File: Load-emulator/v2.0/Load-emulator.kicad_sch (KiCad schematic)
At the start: 29 parts, among them J1 2053380002, J10 533980871, J11 533980871, J12 2053380002, J13 2053380002, J14 2053380002, J2 2053380002, J3 2053380002, J4 2053380002, J5 SSW-126-01-G-D, J7 532610471, J8 SSW-126-01-G-D, Q11 NMOS, U6 LM318H

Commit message: [v2.0 - WIP] Update some things
[UPDATED]
- Added all Schematics;
- Changed the PCB size to be 10x20;
- Updated MOSFETs assignments;
- Added heatsinks;
- Changed order on the Picoblade;
- Small file clean up;
- And some more...

[TO DO]
- Fix/Research how to do the RSense stuff;
- Verify if we still need the -10V;
- Verify this VBus/VBat;
- Verify the difference of EPS2 and EPS²RE radio voltage (6V/5V);
- Complete the entire PCB layout; [! IMPORTANT !]
- Do a better clean up of the files;
- And some more...
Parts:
- removed Q11: NMOS, symbol Simulation_SPICE:NMOS
- removed R4, R5, R6, R7, R8, R9: 0R, symbol Device:R
- removed U6: LM318H, symbol Amplifier_Operational:LM318H
- added HS1: 573100D00000G, symbol Mechanical:Heatsink
- added J1: 2053380002, footprints:2053380002, symbol 2053380002:2053380002
- added Q1: RD3L08DBLHRB, footprints:TRANS_RD3L08DBLHRB, symbol RD3L08DBLHRB:RD3L08DBLHRB
- added U0: LT1492, symbol Amplifier_Operational:LT1492
- C1, C2, R2, R3: now left out of the parts list
- J10: renamed from J8; footprint SSW-126-01-G-D:SAMTEC_SSW-126-01-G-D -> footprints:SAMTEC_SSW-126-01-G-D
- J12: renamed from J11; now left out of the parts list
- J9: renamed from J5; footprint SSW-126-01-G-D:SAMTEC_SSW-126-01-G-D -> footprints:SAMTEC_SSW-126-01-G-D
- J99: renamed from J7; now left out of the parts list
- R1: renamed from R52; now left out of the parts list
- renumbered J10 to J11, J1 to J2, J2 to J3, J3 to J4, J4 to J5, J12 to J6, J13 to J7, J14 to J8
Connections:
- net 3V3_Deployment_ANT is gone; now on net R-3V3_AntDep: J10.35, J10.36
- net 3V3_EPS_Beacon is gone; now on net R-3V3_Beacon_TTC: J10.27, J10.28
- net 5V_Radio_0 is gone; now on net R-5V0_Payload: J3.2, J9.49, J9.50
- net Earth is gone; now on net GND: C1.2, C2.2, R1.2
- net Vbat is gone; now on net R-Vbat: J2.2
- net +10V: now also J99.1, J1.1; no longer J99.2
- net -10V: now also J99.2; no longer J99.1
- net 3V3/1A: now also J12.6; no longer J12.4
- net 3V3/2A: now also J12.4; no longer J12.6
- net 5V/3A: now also J12.3; no longer J12.7
- net 7.4V/0.592A: now also J12.7; no longer J12.3
- net Control: now also U0.3 (+)
- net EPS: now also Q1.2
- net GND: now also J1.2
- net at R1.1: now also Q1.3, U0.2 (-)
- net 3V3_AntDep renamed R-3V3_AntDep
- net 3V3_Beacon renamed R-3V3_Beacon_TTC
- net 3V3_OBDH renamed R-3V3_OBDH
- net 5V0_RadioBeacon renamed R-5V0_RadioBeacon
- net 5V0_RadioMain renamed R-5V0_Payload
- net 5V_Payload renamed S-5V_Payload
- net 6V_Radio_1 renamed S-6V_Radio_1
- net VBus renamed R-Vbat
- new net: Q1.1, U0.1
- no-connect marks 84 -> 82
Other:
- sheet Filter_and_CurrentSink_6x500mA renamed Filter_and_CurrentSink_1x3A
- removed sheet Current Sink 500mA
- removed sheet Low-Pass_Filter_1
- added sheet Filter_and_CurrentSink_1x1A (Filter_and_CurrentSink_1x1A.kicad_sch)
- added sheet Filter_and_CurrentSink_1x1A1 (Filter_and_CurrentSink_1x1A.kicad_sch)
- added sheet Filter_and_CurrentSink_1x3A_1 (Filter_and_CurrentSink_3x1A.kicad_sch)
- added sheet Filter_and_CurrentSink_1x3A_2 (Filter_and_CurrentSink_3x1A.kicad_sch)
- added sheet Filter_and_CurrentSink_2x1A (Filter_and_CurrentSink_2x1A.kicad_sch)
- added sheet Filter_and_CurrentSink_2x1A1 (Filter_and_CurrentSink_2x1A.kicad_sch)
- sheet Filter_and_CurrentSink_1x3A: file Filter_and_CurrentSink_6x500mA.kicad_sch -> Filter_and_CurrentSink_3x1A.kicad_sch
- note added: "1A -> 1 mm 2A -> 1,5 mm 3A -> 2 mm"
- note added: "1A MAX"
- note added: "5V from Radio of ESP²RE"
- note added: "< NEED CONFIRMATION"
- note added: "< R-5V0_RadioBeacon ???"
- note added: "Channel 1 - 6V_Radio_1 (6V/3A)/(5V/3A) Channel 2 - 5V_Radio_0 (5V/3A) Channel 3 - 5V_Payload (5V/3A) Channel 4 - 3V3_Beacon_TTC (3V3/2A) Channel 5 - 3V3_Deployment_ANT (3V3/2A) Channel 6 - 3V3_OBDH (3V3/1A) Channel 7 - VBus (7.4V/0,592A) Channel 8 - GND"
- note added: "POWER"
- note added: "REVIEW THE WIDTH > OF THE TRACES"
- note added: "RSense = Vcontrol/Ieps"
- note added: "Schematic of EPS²RE"
- note added: "V - Verify if we still need -10V"
- note added: "We got two different voltages one from EPS and another from EPS²RE the 6V Radio 1 is 6V, meanwhile the two voltages outputs for the Radio from the ESP²RE is 5V."
- note removed: "1A -> 0,22mm 2A -> 0,57mm 3A -> 1mm"
- note removed: "5V do Radio do ESP²RE +"
- note removed: "< Definir um MOSFET"
- note removed: "<- TTC"
- note removed: "<----------TTC"
- note removed: "Channel 1 - 6V_Radio_1 (6V/3A) Channel 2 - 5V_Radio_0 (5V/3A) Channel 3 - VBus (7.4V/0,592A) Channel 4 - 3V3_OBDH (3V3/1A) Channel 5 - 3V3_Deployment_ANT (3V3/2A) Channel 6 - 3V3_EPS_Beacon (3V3/2A) Channel 7 - 5V_Payload (5V/3A) Channel 8 - GND"
- note removed: "Enable Pin"
- note removed: "GND"
- note removed: "Ieps = Vcontrol/Rsense"
- note removed: "MUDAR ESSE AMPOP PARA LT1492"
- note removed: "Obs: After reduction, max current -> 3A"
- note removed: "Precisa dessa informacao?"
- note removed: "Temos duas tensões diferentes, do EPS e EPS²RE, o 6V_Radio_1 é de 6V, enquanto as duas saidas de tensão para o Rádio via ESP²RE são de 5V."
- note removed: "Voltage Input Pin"
- moved on the sheet: J6, J7, J8, J99, R1

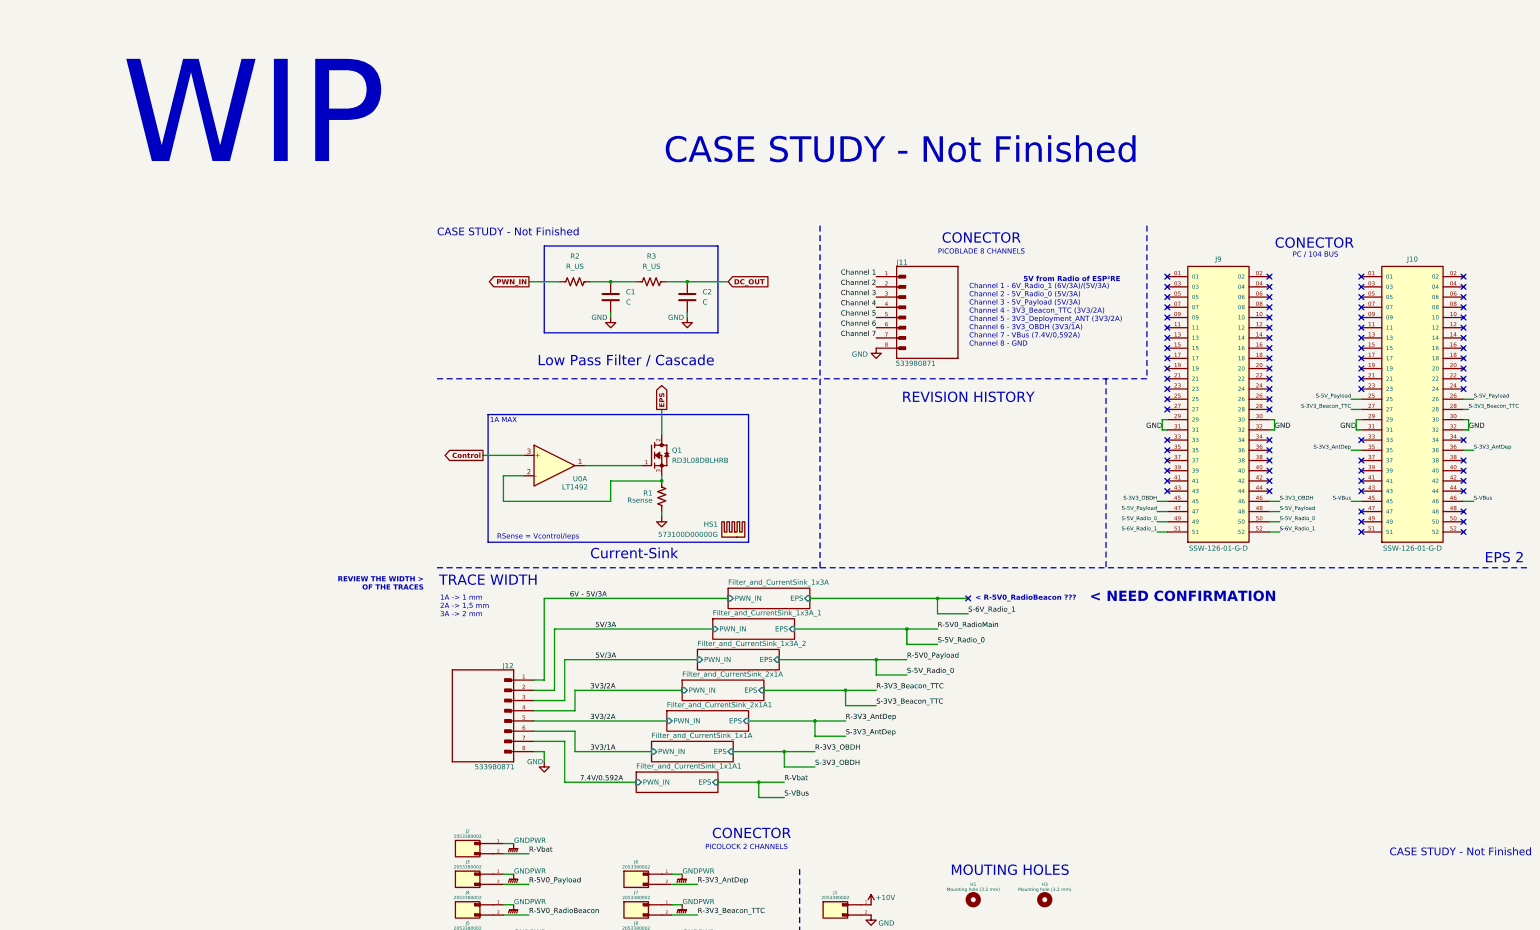
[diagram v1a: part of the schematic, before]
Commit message: [v2.0 - WIP] Added PCB Sketch
[REMOVED]
 - Some comments;

[ADDED]
- 3D models for some components, like heatsinks;
- PCB Sketch (This is just to review how it will look);
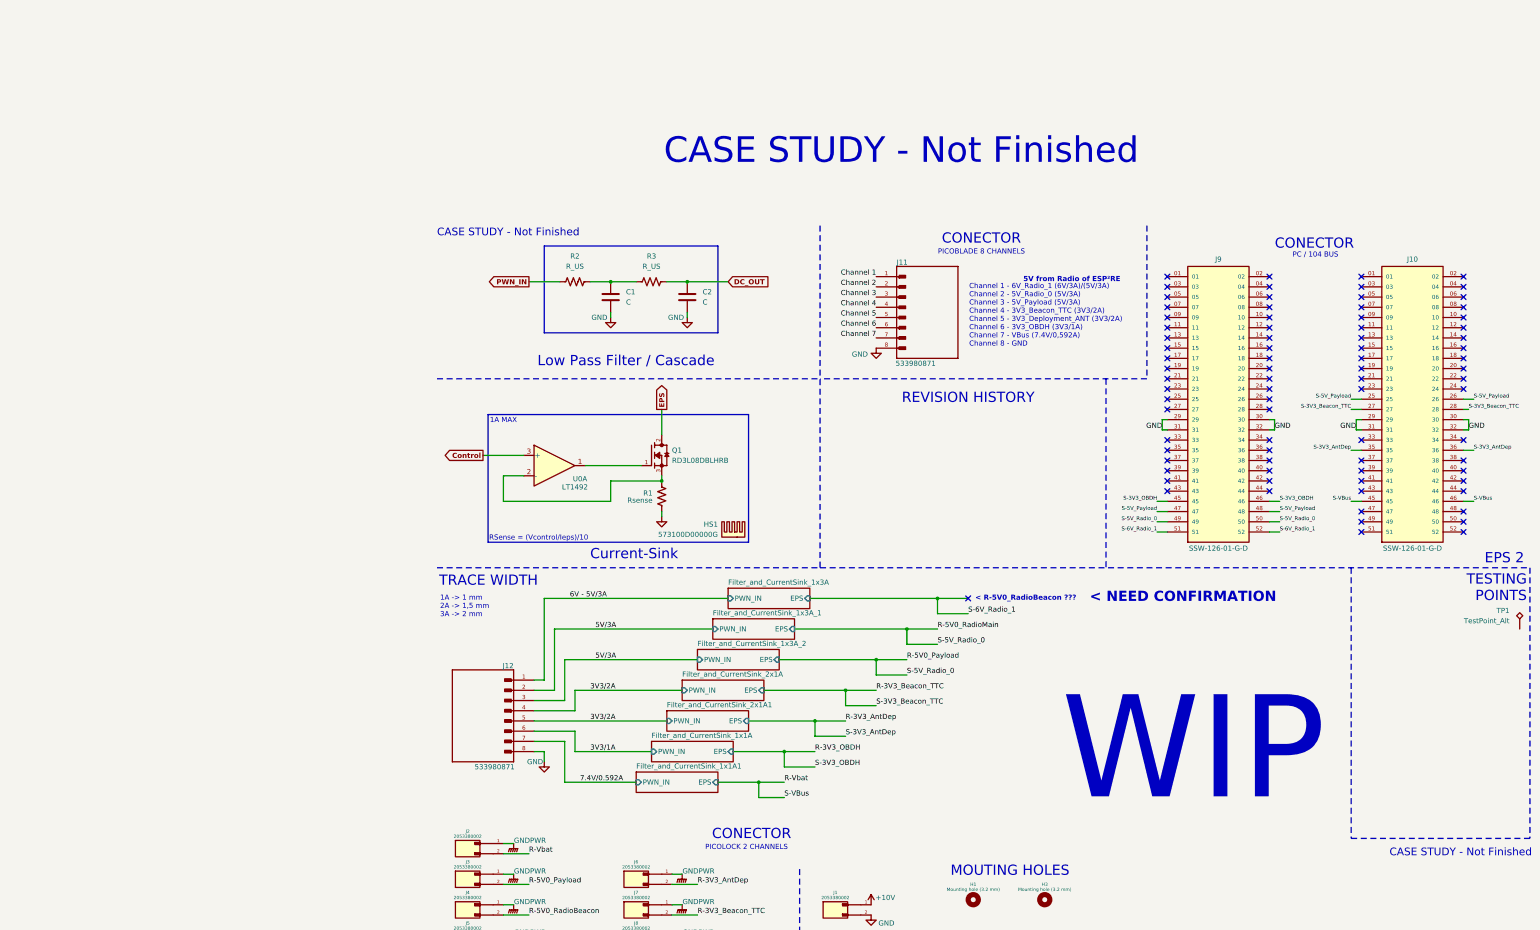
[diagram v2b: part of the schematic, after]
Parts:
- added TP1: TestPoint_Alt, TestPoint:TestPoint_Pad_D1.5mm, symbol Connector:TestPoint_Alt
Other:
- note added: "RSense = (Vcontrol/Ieps)/10"
- note added: "TESTING POINTS"
- note removed: "REVIEW THE WIDTH > OF THE TRACES"
- note removed: "RSense = Vcontrol/Ieps"
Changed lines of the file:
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@@
 	(title_block
 		(title "Load Emulator")
-		(date "2025-09-28")
+		(date "2025-10-03")
 		(rev "v2.0 - WIP")
 		(company "Spacelab")
@@
 		)
 	)
+	(text "TESTING\nPOINTS"
+		(exclude_from_sim no)
+		(at 283.718 99.314 0)
+		(effects
+			(font
+				(size 2.54 2.54)
+				(thickness 0.3175)
+				(color 0 0 0 1)
+			)
+			(justify right top)
+		)
+	)
 	(text "WIP"
 		(exclude_from_sim no)
-		(at 0 0 0)
+		(at 233.68 157.988 0)
 		(effects
 			(font
@@
 		)
 	)
-	(text "RSense = Vcontrol/Ieps"
+	(text "RSense = (Vcontrol/Ieps)/10"
 		(exclude_from_sim no)
-		(at 37.846 90.17 0)
+		(at 25.654 91.186 0)
 		(effects
 			(font
@@
 				(color 0 0 0 1)
 			)
+			(justify left bottom)
 		)
 	)
@@
 		)
 	)
-	(text "REVIEW THE WIDTH >\nOF THE TRACES   "
-		(exclude_from_sim no)
-		(at 9.398 100.076 0)
-		(effects
-			(font
-				(size 1.27 1.27)
-				(thickness 0.254)
-				(bold yes)
-			)
-			(justify right top)
-		)
-	)
 	(junction
 		(at 74.93 26.67)
@@
 		)
 	)
+	(polyline
+		(pts
+			(xy 284.48 97.79) (xy 284.48 165.1)
+		)
+		(stroke
+			(width 0)
+			(type dash)
+			(color 0 0 0 1)
+		)
+	)
 	(wire
 		(pts
@@
 		)
 	)
+	(polyline
+		(pts
+			(xy 240.03 97.79) (xy 240.03 165.1)
+		)
+		(stroke
+			(width 0)
+			(type dash)
+			(color 0 0 0 1)
+		)
+	)
 	(wire
 		(pts
@@
 	(polyline
 		(pts
+			(xy 240.03 165.1) (xy 284.48 165.1)
+		)
+		(stroke
+			(width 0)
+			(type dash)
+			(color 0 0 0 1)
+		)
+	)
+	(polyline
+		(pts
 			(xy 39.37 17.78) (xy 39.37 39.37)
 		)
@@
 			"YQAAAGMAAABlAAAAVAAAAGUAAAB4AAAAdAAAAAkAAAAJAAAACgAAAHAAAABsAAAARQAAAGQAAABp"
 			"AAAAdAAAAG8AAAByAAAALgAAAEkAAABuAAAAdAAAAGUAAAByAAAAYQAAAGMAAAB0AAAAaQAAAHYA"
-			"AABlAAAARQAAAGQAAABpAA=="
+			"AABlAAAARQAAAGQAAABpAAAAOAAAAFoAAABWAAAAUAAAAHQAAABVAAAATQAAAGkAAABJAAAAMAAA"
+			"AEUAAABRAAAAQgAAAEUAAABIAAAAYwAAAFgAAAB4AAAAZwAAAE0AAABoAAAAdAAAADkAAAAvAAAA"
+			"LwAAADcAAAAxAAAAWgAAAHMAAAAyAAAAWQAAAHYAAAB2AAAAZgAAAFIAAABTAAAAawAAAHkAAABa"
+			"AAAATgAAAEQAAABoAAAAOAAAACsAAAByAAAAQwAAAHUAAABNAAAAagAAAHoAAAAvAAAAKwAAAGUA"
+			"AABNAAAAdQAAAFcAAABMAAAAUQAAAHMAAABMAAAAQwAAADQAAAB2AAAAWAAAAFkAAABvAAAAdwAA"
+			"AEIAAAB1AAAASAAAAFQAAABwAAAAVQAAAG0AAABCAAAAZwAAAEkAAABJAAAAQgAAAFAAAABQAAAA"
+			"dgAAAGwAAABFAAAAMwAAACsAAABuAAAAbQAAADUAAABxAAAAWQAAAG8AAABpAAAAcQAAACsAAAB2"
+			"AAAATAAAADQAAABEAAAATQAAAHoAAABFAAAAegAAAHYAAABvAAAAbQAAAFYAAABvAAAANgAAAGYA"
+			"AABDAAAANgAAAFEAAABVAAAARgAAAEIAAABSAAAANAAAADgAAABlAAAANQAAAFgAAAB0AAAAVwAA"
+			"AHIAAABGAAAAZwAAAFIAAABGAAAAQgAAAFIAAABVAAAALwAAAGgAAABhAAAAcQAAAEYAAAA1AAAA"
+			"TQAAAEYAAABYAAAAcAAAADcAAABhAAAAZAAAAG8AAAArAAAAdQAAAEsAAABpAAAAQwAAAFgAAABx"
+			"AAAAVAAAAE4AAAB5AAAAQQAAAGcAAABMAAAAVQAAAG0AAABQAAAAMgAAADIAAABqAAAAMAAAAGYA"
+			"AABpAAAAMgAAAFkAAABhAAAAZgAAAGIAAABiAAAAWgAAAE8AAABvAAAAUwAAADkAAABJAAAAZQAA"
+			"AGcAAABEAAAARQAAADYAAAA5AAAAZgAAAHgAAAA3AAAAUgAAAEkAAAB4AAAATgAAAHgAAABlAAAA"
+			"QQAAAEoAAABnAAAAdgAAAEsAAABpAAAAaQAAAGIAAAB3AAAALwAAAGYAAABtAAAAbgAAAEEAAABL"
+			"AAAARAAAAHoAAABvAAAANQAAAHIAAABJAAAAawAAAG4AAABVAAAATgAAAGkAAAAzAAAANAAAAFEA"
+			"AAA4AAAALwAAAEsAAAAwAAAAWQAAAGsAAAAvAAAAMAAAAGsAAABrAAAATQAAAGUAAABjAAAAMwAA"
+			"AGEAAABqAAAAUAAAAHYAAABpAAAASAAAADQAAABOAAAAZAAAAEUAAABpAAAAWQAAAHAAAAAyAAAA"
+			"TQAAAGIAAABJAAAARgAAAA=="
 		)
 	)
@@
 		(polyline
 			(pts
-				(xy 102.87 160.02) (xy 102.87 170.18) (xy 133.35 170.18) (xy 133.35 196.85) (xy 12.7 196.85) (xy 12.7 160.02)
+				(xy 133.35 170.18) (xy 133.35 196.85) (xy 176.53 196.85) (xy 176.53 170.18)
 			)
 			(stroke
@@
 		(polyline
 			(pts
-				(xy 133.35 170.18) (xy 133.35 196.85) (xy 176.53 196.85) (xy 176.53 170.18)
+				(xy 102.87 160.02) (xy 102.87 170.18) (xy 133.35 170.18) (xy 133.35 196.85) (xy 12.7 196.85) (xy 12.7 160.02)
 			)
 			(stroke
@@
 					(unit 1)
 				)
+			)
+		)
+	)
+	(symbol
+		(lib_id "Connector:TestPoint_Alt")
+		(at 281.94 113.03 0)
+		(mirror y)
+		(unit 1)
+		(exclude_from_sim no)
+		(in_bom yes)
+		(on_board yes)
+		(dnp no)
+		(property "Reference" "TP1"
+			(at 279.4 108.4579 0)
+			(effects
+				(font
+					(size 1.27 1.27)
+				)
+				(justify left)
+			)
+		)
+		(property "Value" "TestPoint_Alt"
+			(at 279.4 110.9979 0)
+			(effects
+				(font
+					(size 1.27 1.27)
+				)
+				(justify left)
+			)
+		)
+		(property "Footprint" "TestPoint:TestPoint_Pad_D1.5mm"
+			(at 276.86 113.03 0)
+			(effects
+				(font
+					(size 1.27 1.27)
+				)
+				(hide yes)
+			)
+		)
+		(property "Datasheet" "~"
+			(at 276.86 113.03 0)
+			(effects
+				(font
+					(size 1.27 1.27)
+				)
+				(hide yes)
+			)
+		)
+		(property "Description" "test point (alternative shape)"
+			(at 281.94 113.03 0)
+			(effects
+				(font
+					(size 1.27 1.27)
+				)
+				(hide yes)
+			)
+		)
+		(pin "1"
+		)
+		(instances
+			(project ""
+				(path "/9054bfd2-3cc0-4c96-aa71-abdb09b76dc7"
+					(reference "TP1")
+					(unit 1)
+				)

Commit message: [v2.0 - WIP] Release Candidate 1. (#6)
Ready for review
- PCB Wired up.
- Schematic ready.

[MISSING]
- Values for some Resistors and Capacitors;
- Verify if EPS conector is correct;
- Change schematic to release.
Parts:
- removed C1, C2: C, symbol Device:C
- removed H1, H2, H3, H4: Mounting hole (3.2 mm), footprints:MountingHole, symbol MountingHole:MountingHole
- removed HS1: 573100D00000G, symbol Mechanical:Heatsink
- removed J11, J12: 533980871, footprints:MOLEX_533980871, symbol 533980871:533980871
- removed J99: 532610471, footprints:532610471, symbol 532610471:532610471
- removed Q1: RD3L08DBLHRB, footprints:TRANS_RD3L08DBLHRB, symbol RD3L08DBLHRB:RD3L08DBLHRB
- removed R1: Rsense, symbol Device:R_US
- removed R2, R3: R_US, symbol Device:R_US
- removed U0: LT1492, symbol Amplifier_Operational:LT1492
- added H1, H2, H3, H4: Mounting Hole (3.2 mm), MountingHole:MountingHole_3.2mm_M3_ISO14580_Pad, symbol Mechanical:MountingHole
- added J9: 533980871, footprints:MOLEX_533980871, symbol 533980871:533980871
- added TP10, TP11, TP12, TP13, TP14, TP15, TP2, TP3, TP4, TP5, TP6, TP7, TP8, TP9: TestPoint_Alt, TestPoint:TestPoint_Pad_D1.5mm, symbol Connector:TestPoint_Alt
- renumbered J2 to J1, J9 to J10, J10 to J11, J3 to J2, J4 to J3, J5 to J4, J6 to J5, J7 to J6, J8 to J7, J1 to J8
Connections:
- net S-5V_Payload is gone; now on net 5V_Payload: J10.47, J10.48, J11.25, J11.26
- net S-6V_Radio_1 is gone; now on net 5V6V_RadioBeacon_1: J10.51, J10.52
- net +10V: now also TP15.1
- net Channel 1: now also J9.1, TP8.1
- net Channel 2: now also J9.2, TP9.1
- net Channel 3: now also J9.3, TP10.1
- net Channel 4: now also J9.4, TP11.1
- net Channel 5: now also J9.5, TP12.1
- net Channel 6: now also J9.6, TP13.1
- net Channel 7: now also J9.7, TP14.1
- net GND: now also J1.1, J5.1, J6.1, J7.1, J9.8
- net GNDPWR: no longer J1.1, J5.1, J6.1, J7.1
- net 5V_Payload: now reaches TP1.1
- net 5V_Payload: now also J2.2
- net R-3V3_AntDep renamed 3V3_AntDep
- net 3V3_AntDep: now also TP4.1
- net R-3V3_Beacon_TTC renamed 3V3_Beacon_TTC
- net 3V3_Beacon_TTC: now also TP5.1
- net R-3V3_OBDH renamed 3V3_OBDH
- net 3V3_OBDH: now also TP6.1
- net R-5V0_Payload renamed 5V_RadioMain_0
- net 5V_RadioMain_0: now also TP3.1; no longer J2.2
- net R-5V0_RadioBeacon renamed 5V6V_RadioBeacon_1
- net 5V6V_RadioBeacon_1: now also TP2.1
- net R-Vbat renamed Vbat_Vbus
- net Vbat_Vbus: now also TP7.1
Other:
- note added: "1A -> 0,5 mm 2A -> 1 mm 3A -> 1,5 mm"
- note added: "3A MAX"
- note added: "Channel 1 - 6V_Radio_1 (6V/3A) - 5V_Radio_Beacon (5V/3A) Channel 2 - 5V_Radio_0/Main (5V/3A) Channel 3 - 5V_Payload (5V/3A) Channel 4 - 3V3_Beacon_TTC (3V3/2A) Channel 5 - 3V3_Deployment_ANT (3V3/2A) Channel 6 - 3V3_OBDH (3V3/1A) Channel 7 - VBus/VBat (7.4V/0,592A) Channel 8 - GND"
- note added: "Current-Sinks"
- note added: "Missing: - Values for both: Resistor and Capacitors, for the 3A Current Sinks; - Check if SSW conector is in the right angle/rotation; - Change the "Revision History" table,"
- note added: "POWER FLAGS"
- note added: "RE²PS"
- note removed: "1A -> 1 mm 2A -> 1,5 mm 3A -> 2 mm"
- note removed: "5V from Radio of ESP²RE"
- note removed: "< NEED CONFIRMATION"
- note removed: "< R-5V0_RadioBeacon ???"
- note removed: "Channel 1 - 6V_Radio_1 (6V/3A)/(5V/3A) Channel 2 - 5V_Radio_0 (5V/3A) Channel 3 - 5V_Payload (5V/3A) Channel 4 - 3V3_Beacon_TTC (3V3/2A) Channel 5 - 3V3_Deployment_ANT (3V3/2A) Channel 6 - 3V3_OBDH (3V3/1A) Channel 7 - VBus (7.4V/0,592A) Channel 8 - GND"
- note removed: "Current-Sink"
- note removed: "EPS²RE"
- note removed: "PICOLOCK 4 CHANNELS"
- note removed: "RSense = (Vcontrol/Ieps)/10"
- note removed: "Schematic of EPS²RE"
- note removed: "V - Verify if we still need -10V"
- note removed: "Vbus"
- note removed: "WIP"
- note removed: "We got two different voltages one from EPS and another from EPS²RE the 6V Radio 1 is 6V, meanwhile the two voltages outputs for the Radio from the ESP²RE is 5V."
- moved on the sheet: TP1

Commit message: v2.0
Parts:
- J1, J2, J3, J4, J5, J6, J7, J8: Manufacturer Order Number (none) -> 2053380002; Type (none) -> SMD
- J10, J11: Manufacturer (none) -> Samtec; Manufacturer Order Number (none) -> SSW-126-01-G-D; Type (none) -> Through Hole
- J9: Manufacturer (none) -> Molex; Manufacturer Order Number (none) -> 533980871; Type (none) -> SMD
- TP1, TP10, TP11, TP12, TP13, TP14, TP15, TP2, TP3, TP4, TP5, TP6, TP7, TP8, TP9: Type (none) -> SMD
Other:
- note removed: "CASE STUDY - Not Finished"
- note removed: "Missing: - Values for both: Resistor and Capacitors, for the 3A Current Sinks; - Check if SSW conector is in the right angle/rotation; - Change the "Revision History" table,"
